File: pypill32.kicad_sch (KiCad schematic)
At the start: 43 parts, among them J1 HeaderR, J2 HeaderL, J4 ISP, SW1 RST_BTN, SW2 BOOT_BTN, U1 SRV05-4, U2 PY32F030F18P6, U3 CH340N, U4 AMS1117-3.3, Y1 32.768 kHz

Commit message: checking and verifying still
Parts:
- added J3: USB_PINS, Connector_PinHeader_2.00mm:PinHeader_1x04_P2.00mm_Vertical, symbol Connector:Conn_01x04_Pin
- C13, C8: value 12p TSEKKAA -> 12p
- J4: value ISP -> SWD_HEADER
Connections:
- net GND: now also J3.4 (Pin_4)
- net PF0: no longer R6.2
- net PF1: no longer R5.2
- net USB_D+: now also J3.3 (Pin_3)
- net USB_D-: now also J3.2 (Pin_2)
- net VBUS: now also J3.1 (Pin_1)
- net PA2 renamed PYUTX
- net PYUTX: now also R6.2
- net PA3 renamed PYURX
- net PYURX: now also R5.2
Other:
- note added: "3V3 linear reg."
- note added: "BOOT button"
- note added: "Fuse & PWR filtering"
- note added: "Licensed under CERN OHL. See the attached LICENSE."
- note added: "PA2=USART1_TX"
- note added: "PA3=USART1_RX"
- note added: "PUYAISP support:"
- note added: "PWR LED"
- note added: "PYPILL32 rev.A"
- note added: "RESET button"
- note added: "SWD header"
- note added: "Set your MCU to bootloader mode by using ONE of the following methods: A) Disconnect your USB-to-serial converter, pull BOOT0 pin (PF4) to VCC (or press and hold the BOOT button, if your board has one), then connect the converter to your USB port. BOOT0 pin (or BOOT button) can be released now. B) Connect your USB-to-serial converter to your USB port. Pull BOOT0 pin (PF4) to VCC, then pull nRST (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"
- note added: "USB ESD protection"
- note added: "USB UART ports PA2/PA3 selected to match with: https://github.com/wagiminator/MCU-Flash-Tools?tab=readme-ov-file#puyaisp"
- note added: "USB-C connector"
- note added: "USB-UART CH340N"
- note removed: "P1=PF0=USART1_RX"
- note removed: "P2=PF1=USART1_TX"
- note removed: "TODO: ------ -USB-pinnireiät? -2,54 jakoon piikkirimat (protolevylle) -- tasajakoon kiinn.ruuvit"
- title: (none) -> pypill32 - indie py32f030 evaluation board
- moved on the sheet: C1, C10, C11, C12, C13, C14, C15, C16, C2, C3, C4, C5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

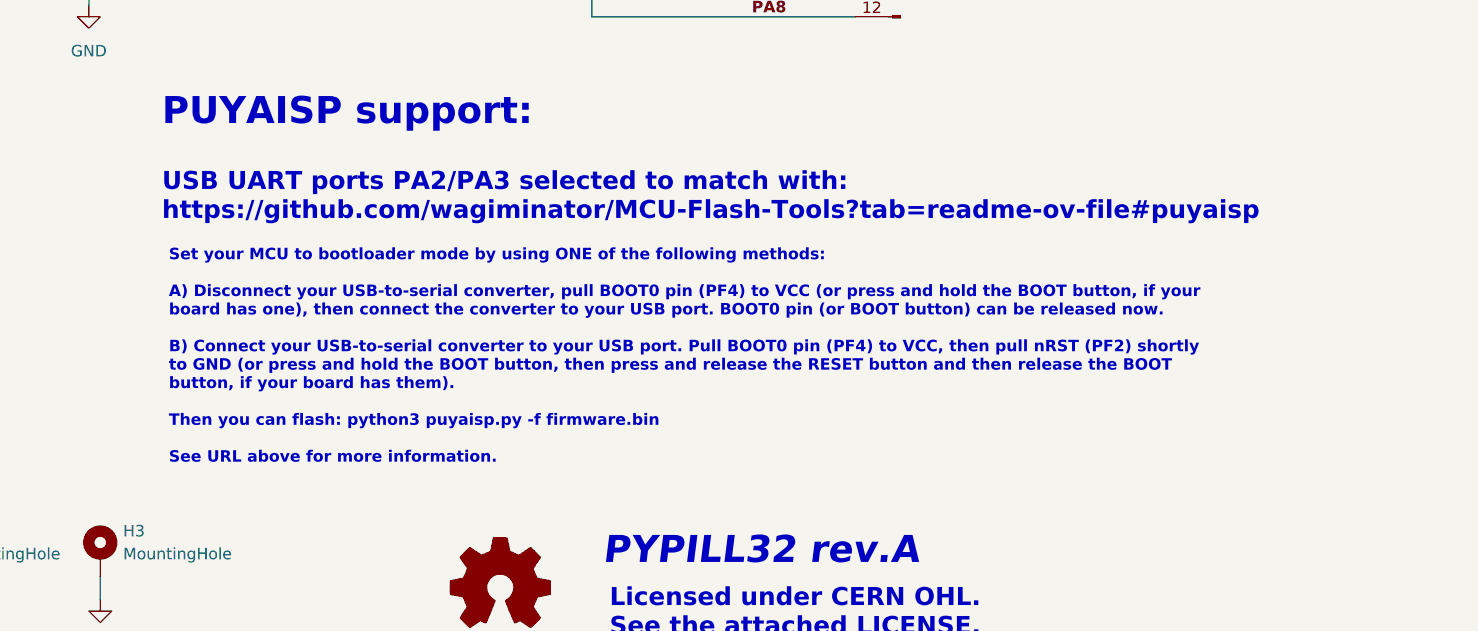
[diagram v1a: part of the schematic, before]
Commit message: schema to pdf
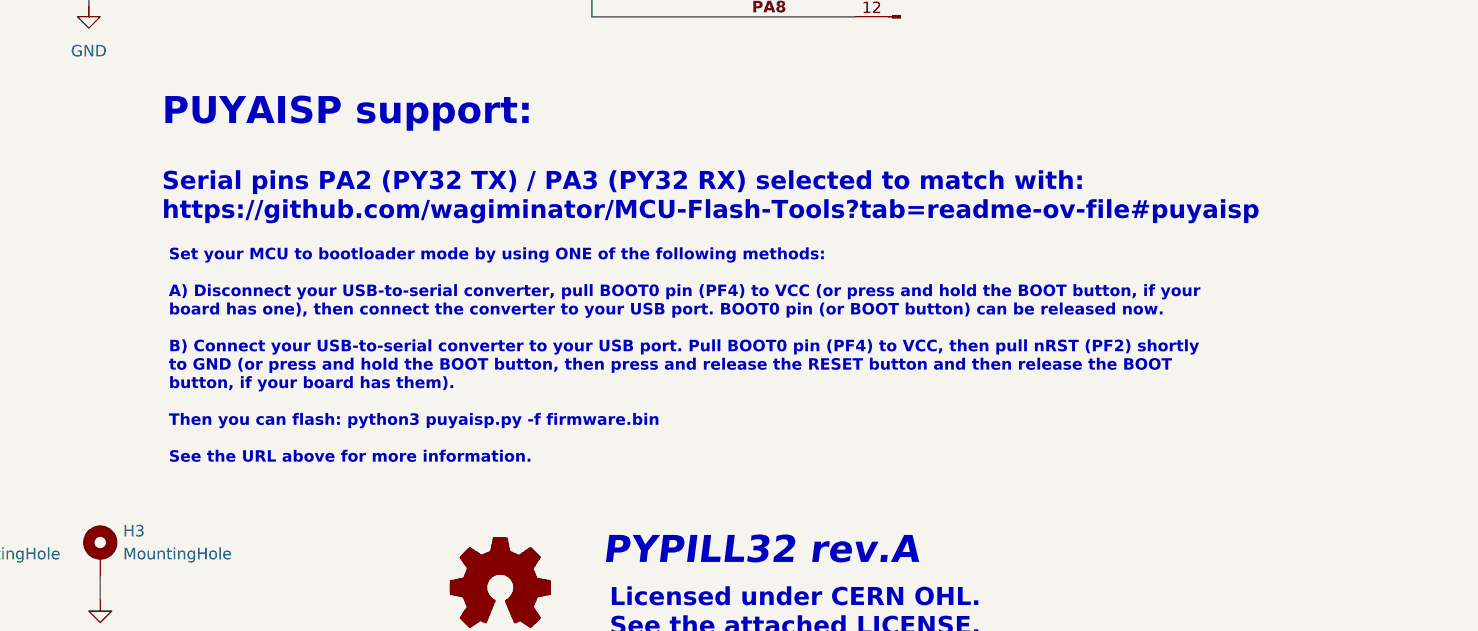
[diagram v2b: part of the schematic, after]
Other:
- note added: "Serial pins PA2 (PY32 TX) / PA3 (PY32 RX) selected to match with: https://github.com/wagiminator/MCU-Flash-Tools?tab=readme-ov-file#puyaisp"
- note removed: "USB UART ports PA2/PA3 selected to match with: https://github.com/wagiminator/MCU-Flash-Tools?tab=readme-ov-file#puyaisp"
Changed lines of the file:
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@@
 		)
 	)
-	(text "USB UART ports PA2/PA3 selected to match with:\nhttps://github.com/wagiminator/MCU-Flash-Tools?tab=readme-ov-file#puyaisp"
+	(text "Serial pins PA2 (PY32 TX) / PA3 (PY32 RX) selected to match with:\nhttps://github.com/wagiminator/MCU-Flash-Tools?tab=readme-ov-file#puyaisp"
 		(exclude_from_sim no)
 		(at 151.638 130.556 0)
@@
 		)
 	)
-	(text "Set your MCU to bootloader mode by using ONE of the following methods:\n\nA) Disconnect your USB-to-serial converter, pull BOOT0 pin (PF4) to VCC (or press and hold the BOOT button, if your \nboard has one), then connect the converter to your USB port. BOOT0 pin (or BOOT button) can be released now.\n\nB) Connect your USB-to-serial converter to your USB port. Pull BOOT0 pin (PF4) to VCC, then pull nRST (PF2) shortly \nto GND (or press and hold the BOOT button, then press and release the RESET button and then release the BOOT \nbutton, if your board has them).\n\nThen you can flash: python3 puyaisp.py -f firmware.bin\n\nSee URL above for more information."
+	(text "Set your MCU to bootloader mode by using ONE of the following methods:\n\nA) Disconnect your USB-to-serial converter, pull BOOT0 pin (PF4) to VCC (or press and hold the BOOT button, if your \nboard has one), then connect the converter to your USB port. BOOT0 pin (or BOOT button) can be released now.\n\nB) Connect your USB-to-serial converter to your USB port. Pull BOOT0 pin (PF4) to VCC, then pull nRST (PF2) shortly \nto GND (or press and hold the BOOT button, then press and release the RESET button and then release the BOOT \nbutton, if your board has them).\n\nThen you can flash: python3 puyaisp.py -f firmware.bin\n\nSee the URL above for more information."
 		(exclude_from_sim no)
 		(at 152.4 148.336 0)

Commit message: LICENSE
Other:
- note added: "This board is licensed under CERN-OHL-W (weakly reciprocal). See the attached LICENSE."
- note removed: "Licensed under CERN OHL. See the attached LICENSE."
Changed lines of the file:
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@@
 		)
 	)
-	(text "Licensed under CERN OHL. \nSee the attached LICENSE."
+	(text "This board is licensed under CERN-OHL-W \n(weakly reciprocal). See the attached LICENSE."
 		(exclude_from_sim no)
-		(at 221.996 176.784 0)
+		(at 201.422 176.53 0)
 		(effects
 			(font
@@
 				(bold yes)
 			)
+			(justify left)
 		)
 	)

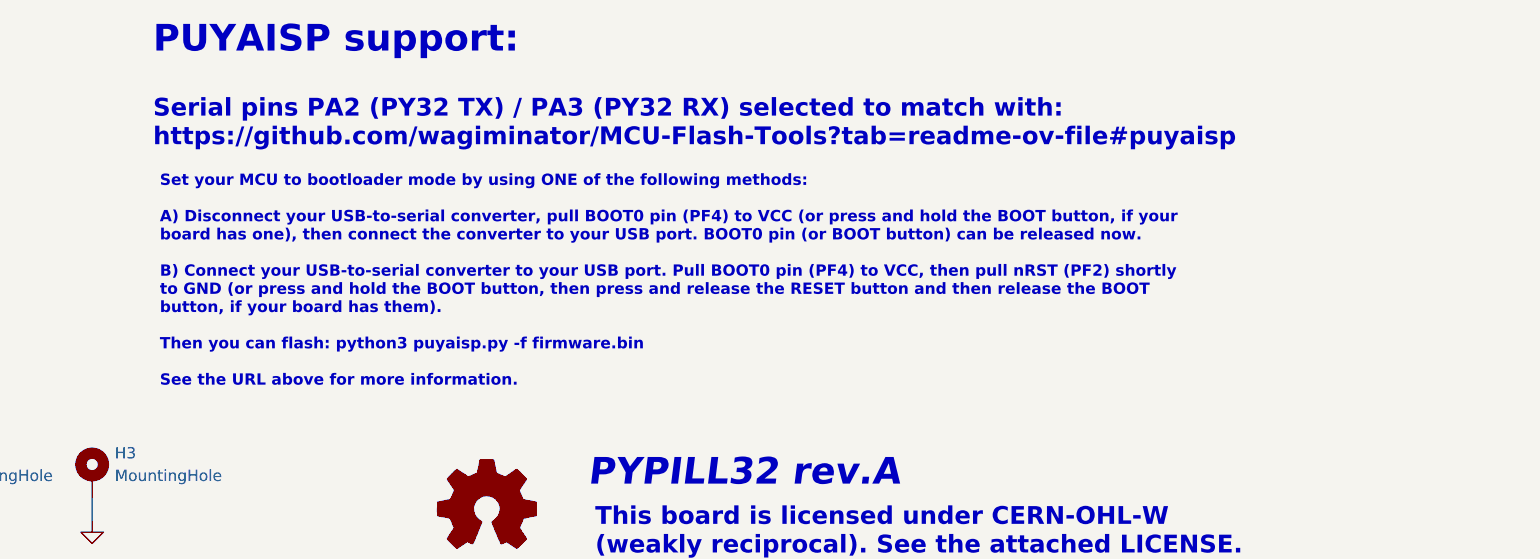
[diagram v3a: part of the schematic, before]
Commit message: note text edit
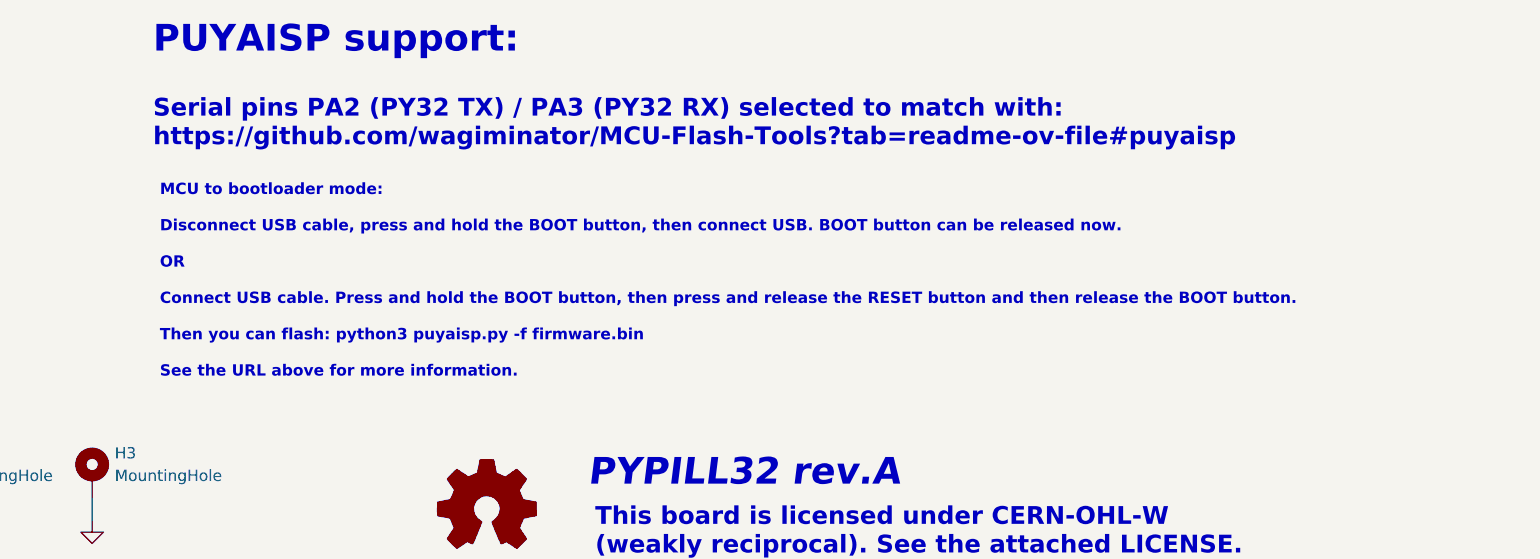
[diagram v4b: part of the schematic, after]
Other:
- note added: "MCU to bootloader mode: Disconnect USB cable, press and hold the BOOT button, then connect USB. BOOT button can be released now. OR Connect USB cable. Press and hold the BOOT button, then press and release the RESET button and then release the BOOT button. Then you can flash: python3 puyaisp.py -f firmware.bin See the URL above for more information."
- note removed: "Set your MCU to bootloader mode by using ONE of the following methods: A) Disconnect your USB-to-serial converter, pull BOOT0 pin (PF4) to VCC (or press and hold the BOOT button, if your board has one), then connect the converter to your USB port. BOOT0 pin (or BOOT button) can be released now. B) Connect your USB-to-serial converter to your USB port. Pull BOOT0 pin (PF4) to VCC, then pull nRST (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"
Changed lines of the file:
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@@
 		)
 	)
-	(text "Set your MCU to bootloader mode by using ONE of the following methods:\n\nA) Disconnect your USB-to-serial converter, pull BOOT0 pin (PF4) to VCC (or press and hold the BOOT button, if your \nboard has one), then connect the converter to your USB port. BOOT0 pin (or BOOT button) can be released now.\n\nB) Connect your USB-to-serial converter to your USB port. Pull BOOT0 pin (PF4) to VCC, then pull nRST (PF2) shortly \nto GND (or press and hold the BOOT button, then press and release the RESET button and then release the BOOT \nbutton, if your board has them).\n\nThen you can flash: python3 puyaisp.py -f firmware.bin\n\nSee the URL above for more information."
+	(text "MCU to bootloader mode:\n\nDisconnect USB cable, press and hold the BOOT button, then connect USB. BOOT button can be released now.\n\nOR\n\nConnect USB cable. Press and hold the BOOT button, then press and release the RESET button and then release the BOOT button.\n\nThen you can flash: python3 puyaisp.py -f firmware.bin\n\nSee the URL above for more information."
 		(exclude_from_sim no)
 		(at 152.4 148.336 0)

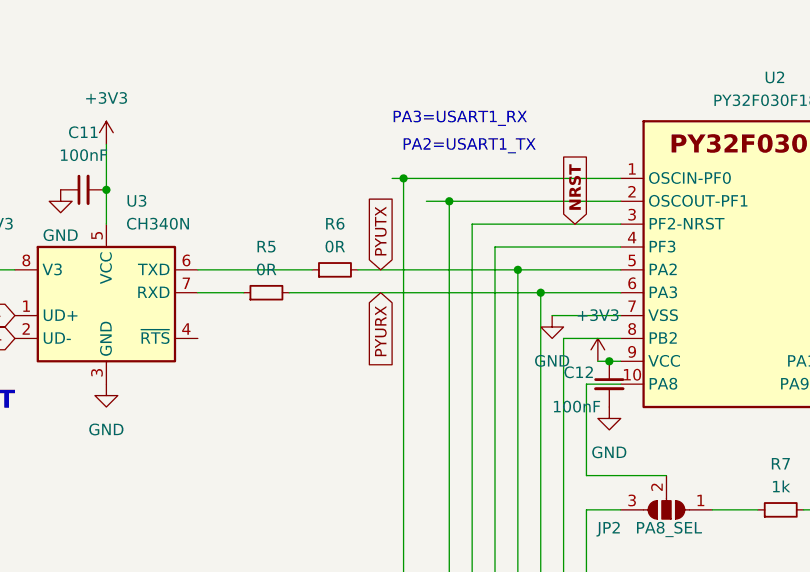
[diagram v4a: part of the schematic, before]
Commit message: fix uart pins
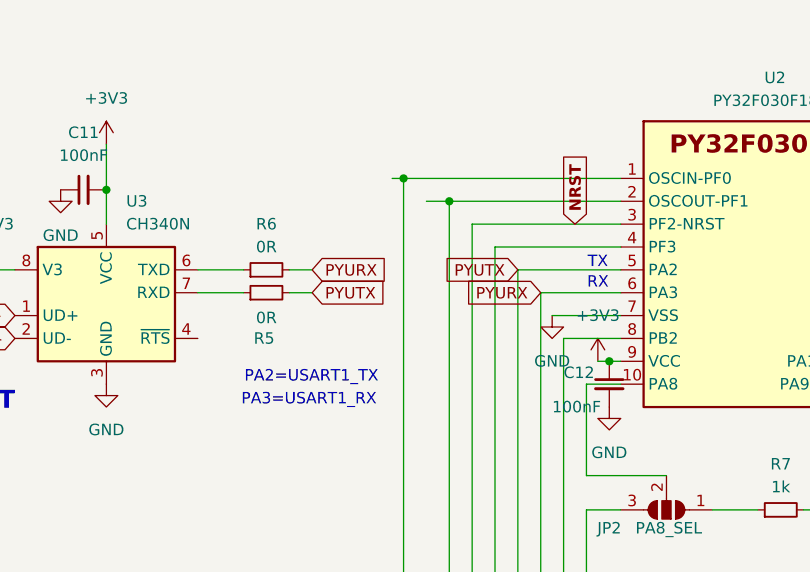
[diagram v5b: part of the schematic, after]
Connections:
- net PYURX: now also R6.2; no longer R5.2
- net PYUTX: now also R5.2; no longer R6.2
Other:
- note added: "RX"
- note added: "TX"
- moved on the sheet: R6
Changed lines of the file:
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@@
 	)
 	(junction
-		(at 191.77 46.99)
-		(diameter 0)
-		(color 0 0 0 0)
-	)
-	(junction
 		(at 81.28 123.19)
 		(diameter 0)
@@
 	)
 	(junction
-		(at 194.31 49.53)
-		(diameter 0)
-		(color 0 0 0 0)
-	)
-	(junction
 		(at 133.35 46.99)
 		(diameter 0)
@@
 	(wire
 		(pts
+			(xy 168.91 49.53) (xy 166.37 49.53)
+		)
+		(stroke
+			(width 0)
+			(type default)
+		)
+	)
+	(wire
+		(pts
 			(xy 134.62 106.68) (xy 138.43 106.68)
 		)
@@
 	(wire
 		(pts
-			(xy 173.99 46.99) (xy 191.77 46.99)
-		)
-		(stroke
-			(width 0)
-			(type default)
-		)
-	)
-	(wire
-		(pts
 			(xy 143.51 106.68) (xy 143.51 109.22)
 		)
@@
 	(wire
 		(pts
-			(xy 156.21 46.99) (xy 168.91 46.99)
+			(xy 156.21 46.99) (xy 161.29 46.99)
 		)
 		(stroke
@@
 	(wire
 		(pts
-			(xy 199.39 59.69) (xy 199.39 69.85)
+			(xy 168.91 46.99) (xy 166.37 46.99)
 		)
 		(stroke
@@
 	(wire
 		(pts
-			(xy 201.93 57.15) (xy 203.2 57.15)
+			(xy 199.39 59.69) (xy 199.39 69.85)
 		)
 		(stroke
@@
 	(wire
 		(pts
-			(xy 69.85 74.93) (xy 50.8 74.93)
+			(xy 201.93 57.15) (xy 203.2 57.15)
 		)
 		(stroke
@@
 	(wire
 		(pts
-			(xy 166.37 49.53) (xy 194.31 49.53)
+			(xy 69.85 74.93) (xy 50.8 74.93)
 		)
 		(stroke
@@
 	(text "PA3=USART1_RX"
 		(exclude_from_sim no)
-		(at 177.8 30.988 0)
+		(at 161.036 62.23 0)
 		(effects
 			(font
@@
 		)
 	)
+	(text "RX"
+		(exclude_from_sim no)
+		(at 200.66 48.514 0)
+		(effects
+			(font
+				(size 1.27 1.27)
+			)
+		)
+	)
 	(text "PA2=USART1_TX"
 		(exclude_from_sim no)
-		(at 193.802 34.036 0)
+		(at 176.276 59.69 0)
 		(effects
 			(font
@@
 		)
 	)
+	(text "TX"
+		(exclude_from_sim no)
+		(at 200.66 46.228 0)
+		(effects
+			(font
+				(size 1.27 1.27)
+			)
+		)
+	)
 	(text "MCU to bootloader mode:\n\nDisconnect USB cable, press and hold the BOOT button, then connect USB. BOOT button can be released now.\n\nOR\n\nConnect USB cable. Press and hold the BOOT button, then press and release the RESET button and then release the BOOT button.\n\nThen you can flash: python3 puyaisp.py -f firmware.bin\n\nSee the URL above for more information."
 		(exclude_from_sim no)
@@
 		)
 	)
+	(global_label "PYURX"
+		(shape input)
+		(at 168.91 46.99 0)
+		(fields_autoplaced yes)
+		(effects
+			(font
+				(size 1.27 1.27)
+			)
+			(justify left)
+		)
+		(property "Intersheetrefs" "${INTERSHEET_REFS}"
+			(at 178.0638 46.99 0)
+			(effects
+				(font
+					(size 1.27 1.27)
+				)
+				(justify left)
+				(hide yes)
+			)
+		)
+	)
 	(global_label "NRST"
 		(shape input)
@@
 		)
 	)
+	(global_label "PYUTX"
+		(shape input)
+		(at 191.77 46.99 180)
+		(fields_autoplaced yes)
+		(effects
+			(font
+				(size 1.27 1.27)
+			)
+			(justify right)
+		)
+		(property "Intersheetrefs" "${INTERSHEET_REFS}"
+			(at 182.9186 46.99 0)
+			(effects
+				(font
+					(size 1.27 1.27)
+				)
+				(justify right)
+				(hide yes)
+			)
+		)
+	)
 	(global_label "USB_D+"
 		(shape input)
@@
 	(global_label "PYUTX"
 		(shape input)
-		(at 176.53 46.99 90)
+		(at 168.91 49.53 0)
 		(fields_autoplaced yes)
 		(effects
@@
 		)
 		(property "Intersheetrefs" "${INTERSHEET_REFS}"
-			(at 176.53 38.1386 90)
+			(at 177.7614 49.53 0)
 			(effects
 				(font
@@
 	(global_label "PYURX"
 		(shape input)
-		(at 176.53 49.53 270)
+		(at 194.31 49.53 180)
 		(fields_autoplaced yes)
 		(effects
@@
 		)
 		(property "Intersheetrefs" "${INTERSHEET_REFS}"
-			(at 176.53 58.6838 90)
+			(at 185.1562 49.53 0)
 			(effects
 				(font
@@
 	(symbol
 		(lib_id "Device:R_Small")
-		(at 171.45 46.99 90)
+		(at 163.83 46.99 90)
 		(unit 1)
 		(exclude_from_sim no)
@@
 		(fields_autoplaced yes)
 		(property "Reference" "R6"
-			(at 171.45 41.91 90)
+			(at 163.83 41.91 90)
 			(effects
 				(font
@@
 		)
 		(property "Value" "0R"
-			(at 171.45 44.45 90)
+			(at 163.83 44.45 90)
 			(effects
 				(font
@@
 		)
 		(property "Footprint" "Resistor_SMD:R_0805_2012Metric_Pad1.20x1.40mm_HandSolder"
-			(at 171.45 46.99 0)
+			(at 163.83 46.99 0)
 			(effects
 				(font
@@
 		)
 		(property "Datasheet" "~"
-			(at 171.45 46.99 0)
+			(at 163.83 46.99 0)
 			(effects
 				(font
@@
 		)
 		(property "Description" ""
-			(at 171.45 46.99 0)
+			(at 163.83 46.99 0)
 			(effects
 				(font
@@
 		(on_board yes)
 		(dnp no)
-		(fields_autoplaced yes)
 		(property "Reference" "R5"
-			(at 163.83 44.45 90)
+			(at 163.576 54.61 90)
 			(effects
 				(font
@@
 		)
 		(property "Value" "0R"
-			(at 163.83 46.99 90)
+			(at 163.83 52.324 90)
 			(effects
 				(font
